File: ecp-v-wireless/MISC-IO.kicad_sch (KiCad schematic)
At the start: 0 parts

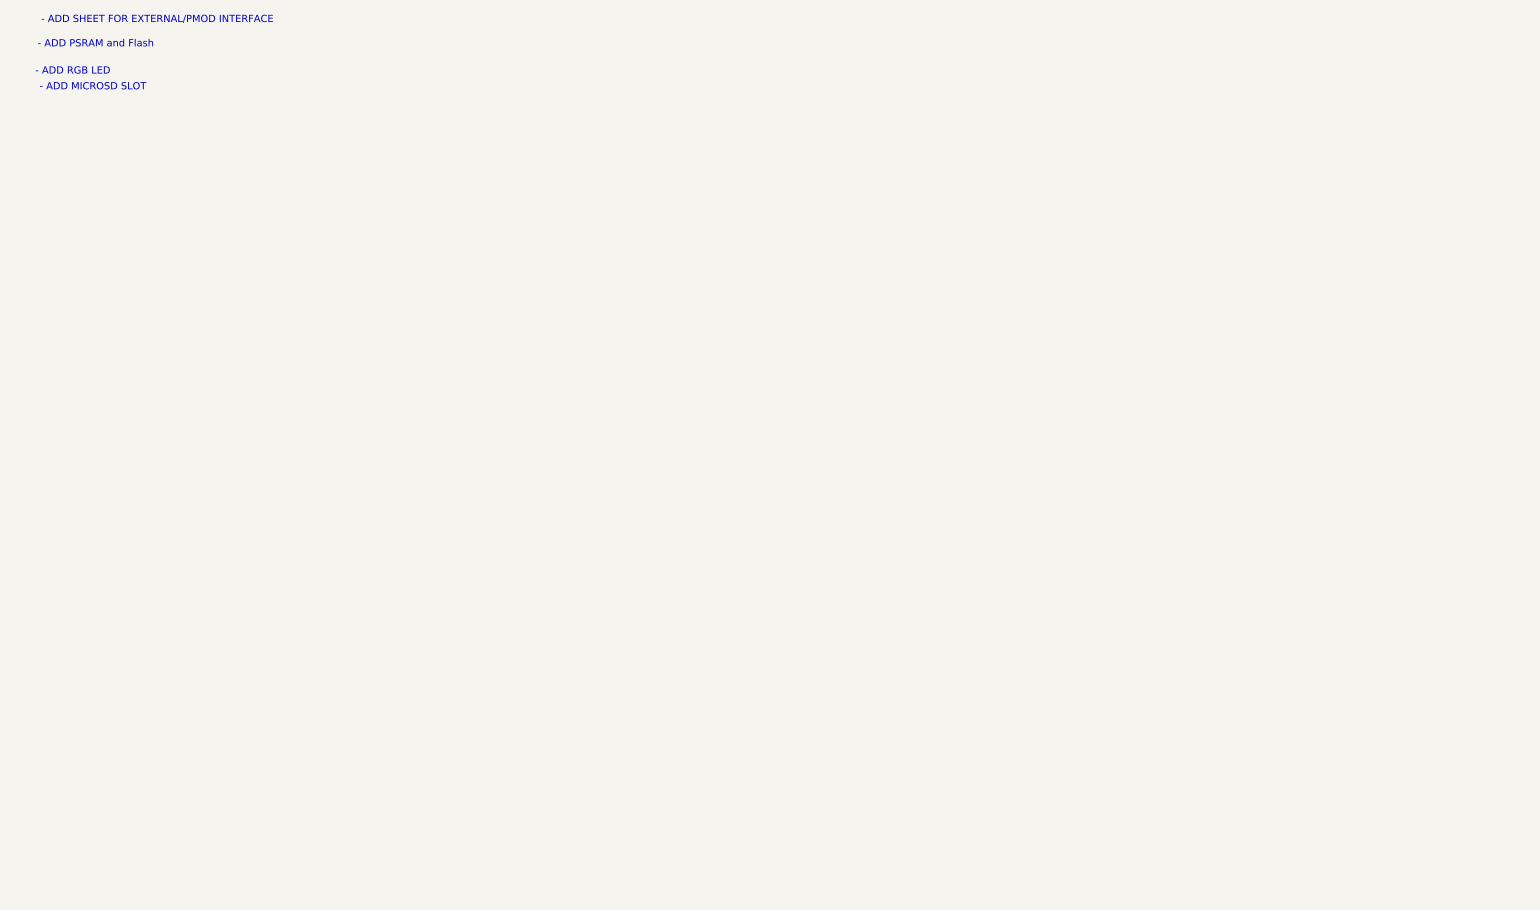
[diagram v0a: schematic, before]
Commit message: Add block diagram, USB, LiPo MGMT, Regs, etc
Signed-off-by: Michael Welling <mwelling79@gmail.com>
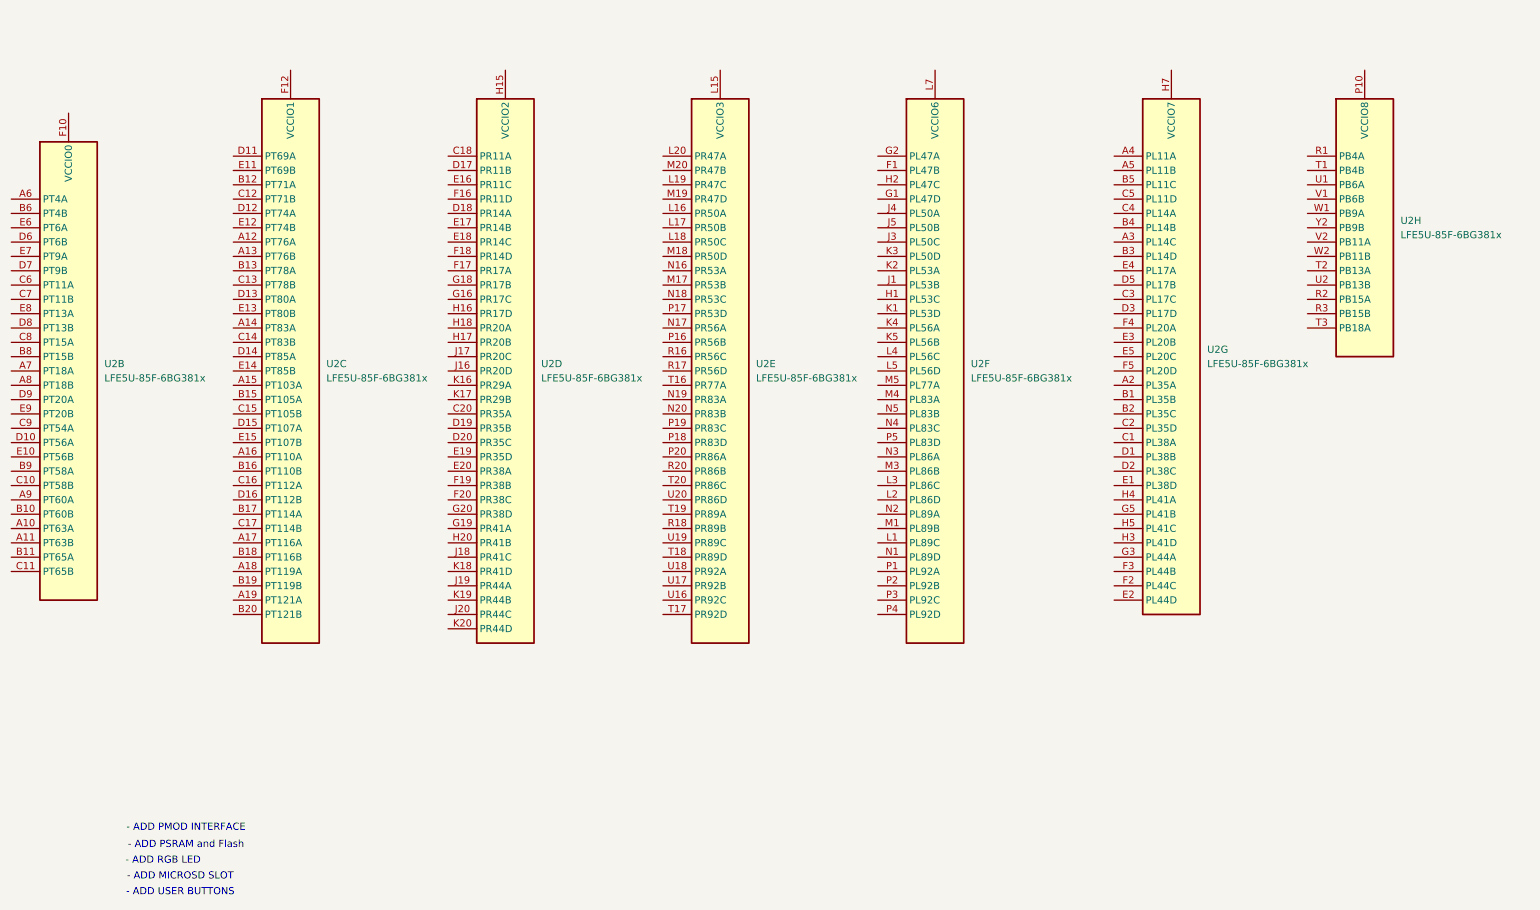
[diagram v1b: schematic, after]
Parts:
- added U2: LFE5U-85F-6BG381x, Package_BGA:Lattice_caBGA-381_17x17mm_Layout20x20_P0.8mm, symbol FPGA_Lattice:LFE5U-85F-6BG381x
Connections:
- new net: U2.H6 (VCCIO7), U2.H7 (VCCIO7), U2.J6 (VCCIO7)
- new net: U2.L14 (VCCIO3), U2.L15 (VCCIO3), U2.M15 (VCCIO3)
- new net: U2.F11 (VCCIO1), U2.F12 (VCCIO1)
- new net: U2.F10 (VCCIO0), U2.F9 (VCCIO0)
- new net: U2.P10 (VCCIO8), U2.P9 (VCCIO8)
- new net: U2.H14 (VCCIO2), U2.H15 (VCCIO2), U2.J15 (VCCIO2)
- new net: U2.L6 (VCCIO6), U2.L7 (VCCIO6), U2.M6 (VCCIO6)
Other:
- note added: "- ADD PMOD INTERFACE"
- note added: "- ADD USER BUTTONS"
- note removed: "- ADD SHEET FOR EXTERNAL/PMOD INTERFACE"
